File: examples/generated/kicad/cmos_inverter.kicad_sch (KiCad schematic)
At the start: 4 parts

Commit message: Attempt shape and wiring fixes again.
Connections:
- net GND: no longer MN1.3 (S), MP1.1 (D), MP1.3 (S), VDD.2 (E2)
- new net: MN1.3 (S), MP1.3 (S)
- new net VDD: MP1.1 (D), VDD.2 (E2)
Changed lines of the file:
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@@
     )
   )
-  (wire (pts (xy 50.00 62.38) (xy 50.00 50.38))
+  (wire (pts (xy 50.00 62.38) (xy 50.00 60.50))
     (stroke (width 0) (type solid) (color 0 0 0 0))
   )
-  (wire (pts (xy 50.00 77.62) (xy 50.00 89.62))
+  (wire (pts (xy 50.00 60.50) (xy 56.00 60.50))
     (stroke (width 0) (type solid) (color 0 0 0 0))
   )
-  (wire (pts (xy 50.00 117.62) (xy 50.00 129.62))
+  (wire (pts (xy 56.00 60.50) (xy 56.00 50.38))
     (stroke (width 0) (type solid) (color 0 0 0 0))
   )
-  (wire (pts (xy 152.54 95.08) (xy 152.54 89.08))
+  (wire (pts (xy 56.00 50.38) (xy 50.00 50.38))
     (stroke (width 0) (type solid) (color 0 0 0 0))
   )
-  (wire (pts (xy 152.54 89.08) (xy 140.54 89.08))
+  (wire (pts (xy 50.00 77.62) (xy 50.00 79.50))
     (stroke (width 0) (type solid) (color 0 0 0 0))
   )
-  (wire (pts (xy 155.08 95.08) (xy 159.50 95.08))
+  (wire (pts (xy 50.00 79.50) (xy 56.00 79.50))
     (stroke (width 0) (type solid) (color 0 0 0 0))
   )
-  (wire (pts (xy 159.50 95.08) (xy 159.50 89.08))
+  (wire (pts (xy 56.00 79.50) (xy 56.00 89.62))
     (stroke (width 0) (type solid) (color 0 0 0 0))
   )
-  (wire (pts (xy 159.50 89.08) (xy 167.08 89.08))
+  (wire (pts (xy 56.00 89.62) (xy 50.00 89.62))
     (stroke (width 0) (type solid) (color 0 0 0 0))
   )
-  (wire (pts (xy 152.54 132.92) (xy 152.54 138.92))
+  (wire (pts (xy 50.00 117.62) (xy 50.00 119.50))
     (stroke (width 0) (type solid) (color 0 0 0 0))
   )
-  (wire (pts (xy 152.54 138.92) (xy 140.54 138.92))
+  (wire (pts (xy 50.00 119.50) (xy 56.00 119.50))
     (stroke (width 0) (type solid) (color 0 0 0 0))
   )
-  (wire (pts (xy 155.08 132.92) (xy 159.50 132.92))
+  (wire (pts (xy 56.00 119.50) (xy 56.00 129.62))
     (stroke (width 0) (type solid) (color 0 0 0 0))
   )
-  (wire (pts (xy 159.50 132.92) (xy 159.50 138.92))
+  (wire (pts (xy 56.00 129.62) (xy 50.00 129.62))
     (stroke (width 0) (type solid) (color 0 0 0 0))
   )
-  (wire (pts (xy 159.50 138.92) (xy 167.08 138.92))
+  (wire (pts (xy 152.54 95.08) (xy 152.54 96.08))
     (stroke (width 0) (type solid) (color 0 0 0 0))
   )
-  (wire (pts (xy 50.00 102.38) (xy 50.00 114.00))
+  (wire (pts (xy 152.54 96.08) (xy 146.54 96.08))
     (stroke (width 0) (type solid) (color 0 0 0 0))
   )
-  (wire (pts (xy 50.00 114.00) (xy 101.25 114.00))
+  (wire (pts (xy 146.54 96.08) (xy 146.54 89.08))
+    (stroke (width 0) (type solid) (color 0 0 0 0))
+  )
+  (wire (pts (xy 146.54 89.08) (xy 140.54 89.08))
+    (stroke (width 0) (type solid) (color 0 0 0 0))
+  )
+  (wire (pts (xy 155.08 95.08) (xy 173.08 95.08))
+    (stroke (width 0) (type solid) (color 0 0 0 0))
+  )
+  (wire (pts (xy 173.08 95.08) (xy 173.08 89.08))
+    (stroke (width 0) (type solid) (color 0 0 0 0))
+  )
+  (wire (pts (xy 173.08 89.08) (xy 167.08 89.08))
+    (stroke (width 0) (type solid) (color 0 0 0 0))
+  )
+  (wire (pts (xy 152.54 132.92) (xy 152.54 131.92))
+    (stroke (width 0) (type solid) (color 0 0 0 0))
+  )
+  (wire (pts (xy 152.54 131.92) (xy 146.54 131.92))
+    (stroke (width 0) (type solid) (color 0 0 0 0))
+  )
+  (wire (pts (xy 146.54 131.92) (xy 146.54 138.92))
+    (stroke (width 0) (type solid) (color 0 0 0 0))
+  )
+  (wire (pts (xy 146.54 138.92) (xy 140.54 138.92))
+    (stroke (width 0) (type solid) (color 0 0 0 0))
+  )
+  (wire (pts (xy 155.08 132.92) (xy 173.08 132.92))
+    (stroke (width 0) (type solid) (color 0 0 0 0))
+  )
+  (wire (pts (xy 173.08 132.92) (xy 173.08 138.92))
+    (stroke (width 0) (type solid) (color 0 0 0 0))
+  )
+  (wire (pts (xy 173.08 138.92) (xy 167.08 138.92))
+    (stroke (width 0) (type solid) (color 0 0 0 0))
+  )
+  (wire (pts (xy 50.00 102.38) (xy 50.00 100.50))
+    (stroke (width 0) (type solid) (color 0 0 0 0))
+  )
+  (wire (pts (xy 50.00 100.50) (xy 101.25 100.50))
+    (stroke (width 0) (type solid) (color 0 0 0 0))
+  )
+  (wire (pts (xy 101.25 100.50) (xy 101.25 114.00))
     (stroke (width 0) (type solid) (color 0 0 0 0))
   )
@@
     (stroke (width 0) (type solid) (color 0 0 0 0))
   )
-  (wire (pts (xy 152.54 84.92) (xy 152.54 143.08))
+  (wire (pts (xy 152.54 84.92) (xy 152.54 82.00))
     (stroke (width 0) (type solid) (color 0 0 0 0))
   )
+  (wire (pts (xy 152.54 82.00) (xy 159.50 82.00))
+    (stroke (width 0) (type solid) (color 0 0 0 0))
+  )
+  (wire (pts (xy 159.50 82.00) (xy 159.50 146.00))
+    (stroke (width 0) (type solid) (color 0 0 0 0))
+  )
+  (wire (pts (xy 159.50 146.00) (xy 152.54 146.00))
+    (stroke (width 0) (type solid) (color 0 0 0 0))
+  )
+  (wire (pts (xy 152.54 146.00) (xy 152.54 143.08))
+    (stroke (width 0) (type solid) (color 0 0 0 0))
+  )

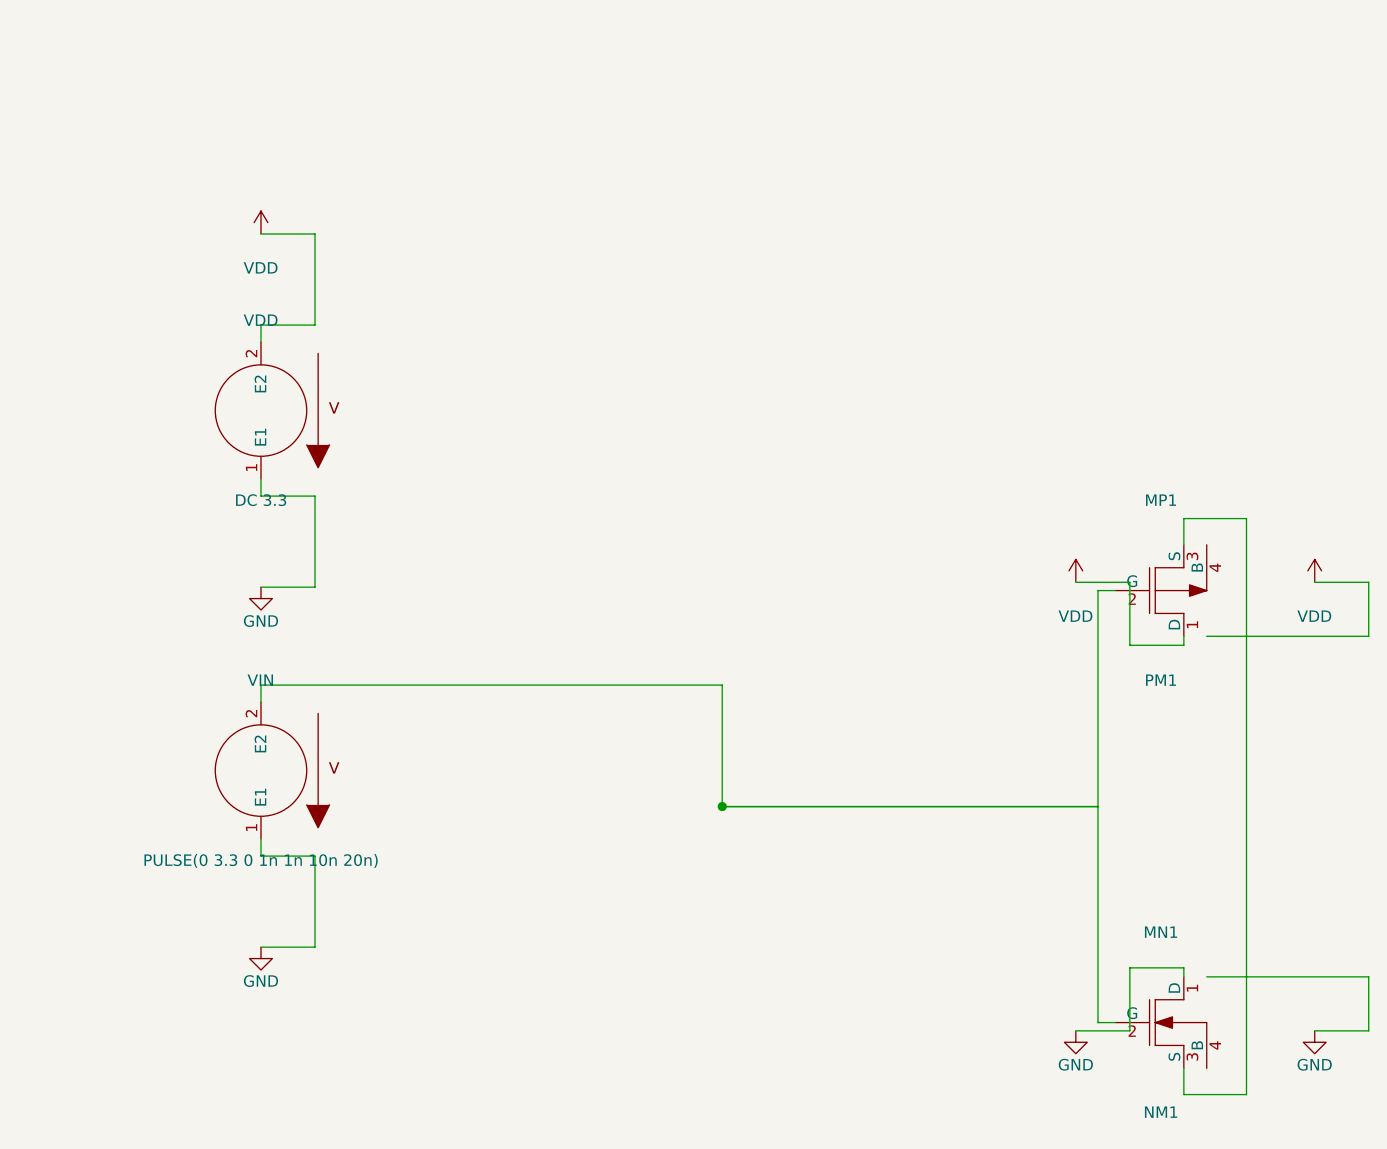
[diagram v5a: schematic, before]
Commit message: Attempt to fix kinking and terminal direction issuses.
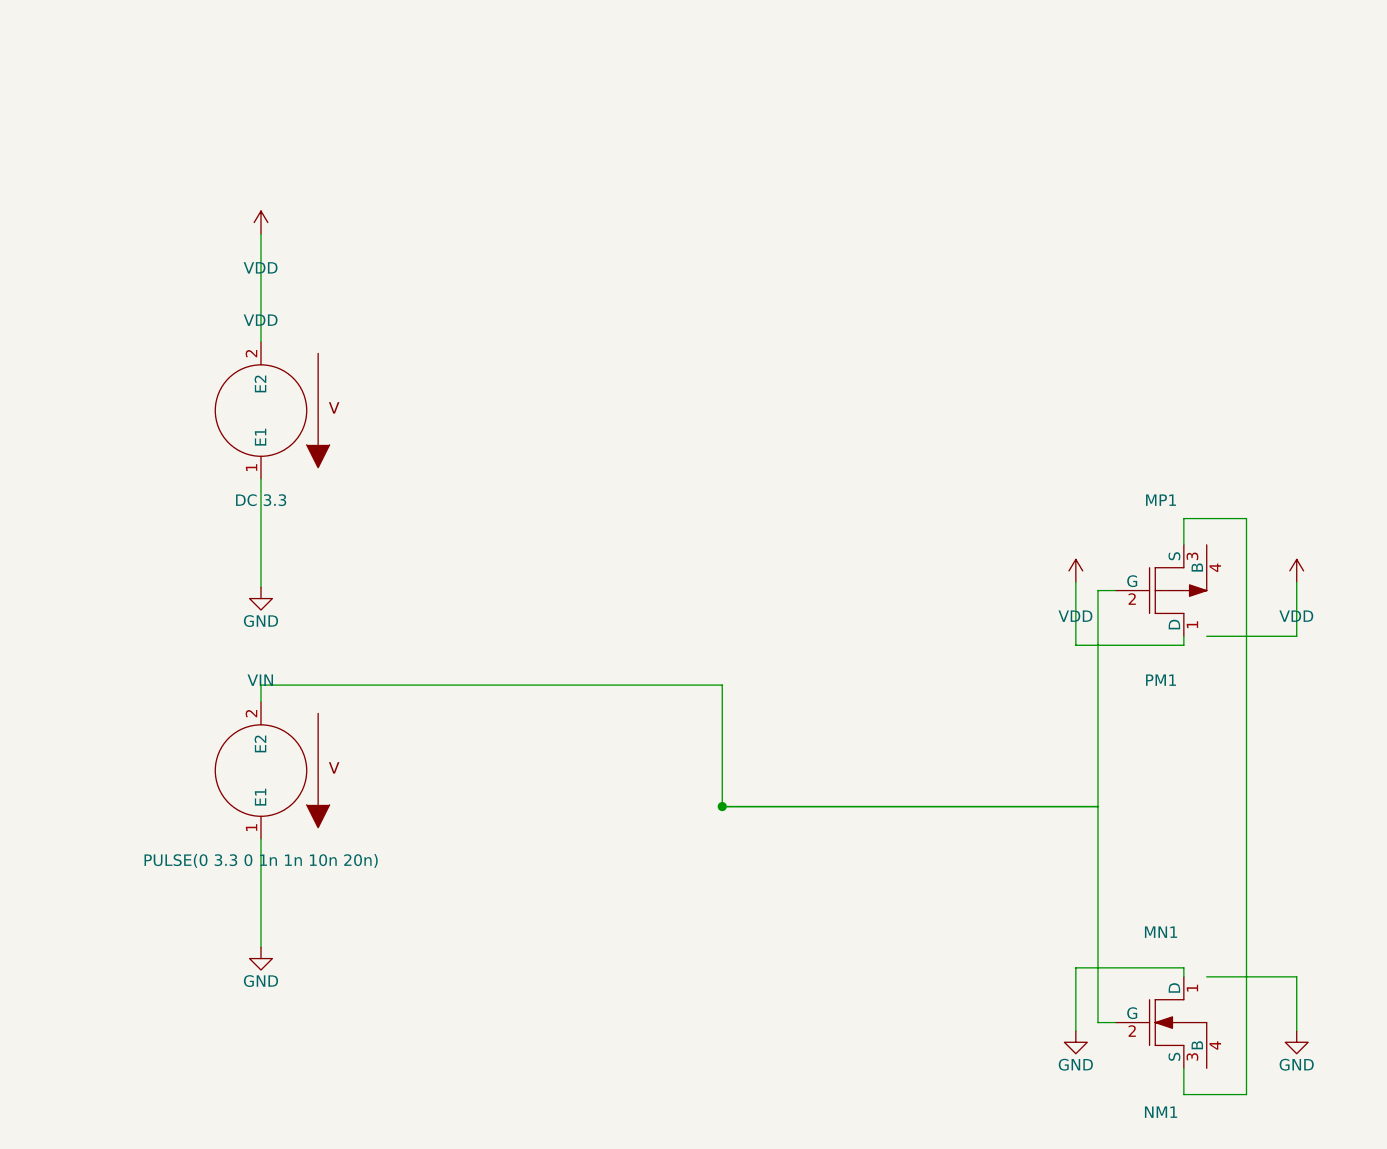
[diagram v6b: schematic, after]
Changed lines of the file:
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@@
     )
   )
-  (symbol (lib_id "VCC") (at 167.08 89.08 0) (unit 1)
+  (symbol (lib_id "VCC") (at 165.08 89.08 0) (unit 1)
     (in_bom yes) (on_board yes)
-    (property "Reference" "#PWR0005" (at 167.08 85.27 0)
+    (property "Reference" "#PWR0005" (at 165.08 85.27 0)
       (effects (font (size 1.27 1.27)) hide)
     )
-    (property "Value" "VDD" (at 167.08 92.89 0)
+    (property "Value" "VDD" (at 165.08 92.89 0)
       (effects (font (size 1.27 1.27)))
     )
@@
     )
   )
-  (symbol (lib_id "GND") (at 167.08 138.92 0) (unit 1)
+  (symbol (lib_id "GND") (at 165.08 138.92 0) (unit 1)
     (in_bom yes) (on_board yes)
-    (property "Reference" "#PWR0007" (at 167.08 135.10999999999999 0)
+    (property "Reference" "#PWR0007" (at 165.08 135.10999999999999 0)
       (effects (font (size 1.27 1.27)) hide)
     )
-    (property "Value" "GND" (at 167.08 142.73 0)
+    (property "Value" "GND" (at 165.08 142.73 0)
       (effects (font (size 1.27 1.27)))
     )
@@
     )
   )
-  (wire (pts (xy 50.00 62.38) (xy 50.00 60.50))
+  (wire (pts (xy 50.00 62.38) (xy 50.00 50.38))
     (stroke (width 0) (type solid) (color 0 0 0 0))
   )
-  (wire (pts (xy 50.00 60.50) (xy 56.00 60.50))
+  (wire (pts (xy 50.00 77.62) (xy 50.00 89.62))
     (stroke (width 0) (type solid) (color 0 0 0 0))
   )
-  (wire (pts (xy 56.00 60.50) (xy 56.00 50.38))
-    (stroke (width 0) (type solid) (color 0 0 0 0))
-  )
-  (wire (pts (xy 56.00 50.38) (xy 50.00 50.38))
-    (stroke (width 0) (type solid) (color 0 0 0 0))
-  )
-  (wire (pts (xy 50.00 77.62) (xy 50.00 79.50))
-    (stroke (width 0) (type solid) (color 0 0 0 0))
-  )
-  (wire (pts (xy 50.00 79.50) (xy 56.00 79.50))
-    (stroke (width 0) (type solid) (color 0 0 0 0))
-  )
-  (wire (pts (xy 56.00 79.50) (xy 56.00 89.62))
-    (stroke (width 0) (type solid) (color 0 0 0 0))
-  )
-  (wire (pts (xy 56.00 89.62) (xy 50.00 89.62))
-    (stroke (width 0) (type solid) (color 0 0 0 0))
-  )
-  (wire (pts (xy 50.00 117.62) (xy 50.00 119.50))
-    (stroke (width 0) (type solid) (color 0 0 0 0))
-  )
-  (wire (pts (xy 50.00 119.50) (xy 56.00 119.50))
-    (stroke (width 0) (type solid) (color 0 0 0 0))
-  )
-  (wire (pts (xy 56.00 119.50) (xy 56.00 129.62))
-    (stroke (width 0) (type solid) (color 0 0 0 0))
-  )
-  (wire (pts (xy 56.00 129.62) (xy 50.00 129.62))
+  (wire (pts (xy 50.00 117.62) (xy 50.00 129.62))
     (stroke (width 0) (type solid) (color 0 0 0 0))
   )
@@
     (stroke (width 0) (type solid) (color 0 0 0 0))
   )
-  (wire (pts (xy 152.54 96.08) (xy 146.54 96.08))
+  (wire (pts (xy 152.54 96.08) (xy 140.54 96.08))
     (stroke (width 0) (type solid) (color 0 0 0 0))
   )
-  (wire (pts (xy 146.54 96.08) (xy 146.54 89.08))
+  (wire (pts (xy 140.54 96.08) (xy 140.54 89.08))
     (stroke (width 0) (type solid) (color 0 0 0 0))
   )
-  (wire (pts (xy 146.54 89.08) (xy 140.54 89.08))
+  (wire (pts (xy 155.08 95.08) (xy 165.08 95.08))
     (stroke (width 0) (type solid) (color 0 0 0 0))
   )
-  (wire (pts (xy 155.08 95.08) (xy 173.08 95.08))
-    (stroke (width 0) (type solid) (color 0 0 0 0))
-  )
-  (wire (pts (xy 173.08 95.08) (xy 173.08 89.08))
-    (stroke (width 0) (type solid) (color 0 0 0 0))
-  )
-  (wire (pts (xy 173.08 89.08) (xy 167.08 89.08))
+  (wire (pts (xy 165.08 95.08) (xy 165.08 89.08))
     (stroke (width 0) (type solid) (color 0 0 0 0))
   )
@@
     (stroke (width 0) (type solid) (color 0 0 0 0))
   )
-  (wire (pts (xy 152.54 131.92) (xy 146.54 131.92))
+  (wire (pts (xy 152.54 131.92) (xy 140.54 131.92))
     (stroke (width 0) (type solid) (color 0 0 0 0))
   )
-  (wire (pts (xy 146.54 131.92) (xy 146.54 138.92))
+  (wire (pts (xy 140.54 131.92) (xy 140.54 138.92))
     (stroke (width 0) (type solid) (color 0 0 0 0))
   )
-  (wire (pts (xy 146.54 138.92) (xy 140.54 138.92))
+  (wire (pts (xy 155.08 132.92) (xy 165.08 132.92))
     (stroke (width 0) (type solid) (color 0 0 0 0))
   )
-  (wire (pts (xy 155.08 132.92) (xy 173.08 132.92))
+  (wire (pts (xy 165.08 132.92) (xy 165.08 138.92))
     (stroke (width 0) (type solid) (color 0 0 0 0))
   )
-  (wire (pts (xy 173.08 132.92) (xy 173.08 138.92))
-    (stroke (width 0) (type solid) (color 0 0 0 0))
-  )
-  (wire (pts (xy 173.08 138.92) (xy 167.08 138.92))
-    (stroke (width 0) (type solid) (color 0 0 0 0))
-  )
